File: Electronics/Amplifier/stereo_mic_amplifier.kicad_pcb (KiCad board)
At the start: 2 copper layers, 34.2 x 45.3 mm, 26 parts, among them P1 mic_L, P2 mic_R, P3 batt, P4 CONN_01X03, U1 TL072

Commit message: Updated layout & cnc files
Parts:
- moved C1 71.1 mm to (37.7, 35.7)
- moved C2 71.1 mm to (58.0, 58.5)
- moved C6 71.1 mm to (37.7, 50.9)
- moved C7 71.1 mm to (47.2, 57.1)
- moved C8 71.1 mm to (51.2, 69.8)
- moved D1 71.1 mm to (40.0, 57.0)
- moved D2 71.1 mm to (65.8, 57.4)
- moved P1 71.1 mm to (46.9, 34.7)
- moved P2 71.1 mm to (47.1, 63.1)
- moved P3 71.1 mm to (38.0, 60.8)
- moved P4 71.1 mm to (56.8, 71.5)
- moved R1 71.1 mm to (42.3, 46.2)
- moved R2 71.1 mm to (48.5, 60.1)
- moved R5 71.1 mm to (39.9, 69.1)
- moved R8 71.1 mm to (43.7, 69.2)
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
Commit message: rotated gerber
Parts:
- moved C1 39.6 mm to (41.0, 75.1), turned to 270 degrees
- moved R5 34.7 mm to (74.4, 73.0), turned to 0 degrees
- moved C3 33.6 mm to (48.6, 75.1), turned to 270 degrees
- moved P1 32.1 mm to (39.9, 66.0), turned to 0 degrees
- moved P3 31.4 mm to (66.1, 74.9), turned to 180 degrees
- moved R8 30.8 mm to (74.5, 69.2), turned to 180 degrees
- moved C6 30.4 mm to (56.2, 75.1), turned to 270 degrees
- moved D1 27.3 mm to (62.3, 72.8), turned to 90 degrees
- moved C4 26.8 mm to (40.4, 57.5), turned to 270 degrees
- moved R1 26.0 mm to (51.5, 70.5), turned to 180 degrees
- moved C8 25.3 mm to (75.1, 61.7), turned to 0 degrees
- moved P4 25.3 mm to (76.8, 56.1), turned to 180 degrees
- moved R4 25.0 mm to (48.2, 67.8), turned to 180 degrees
- moved R9 23.4 mm to (74.6, 48.1), turned to 0 degrees
- moved P2 21.4 mm to (68.4, 65.7), turned to 180 degrees
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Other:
- board size 34.2 x 45.3 mm -> 45.3 x 34.2 mm

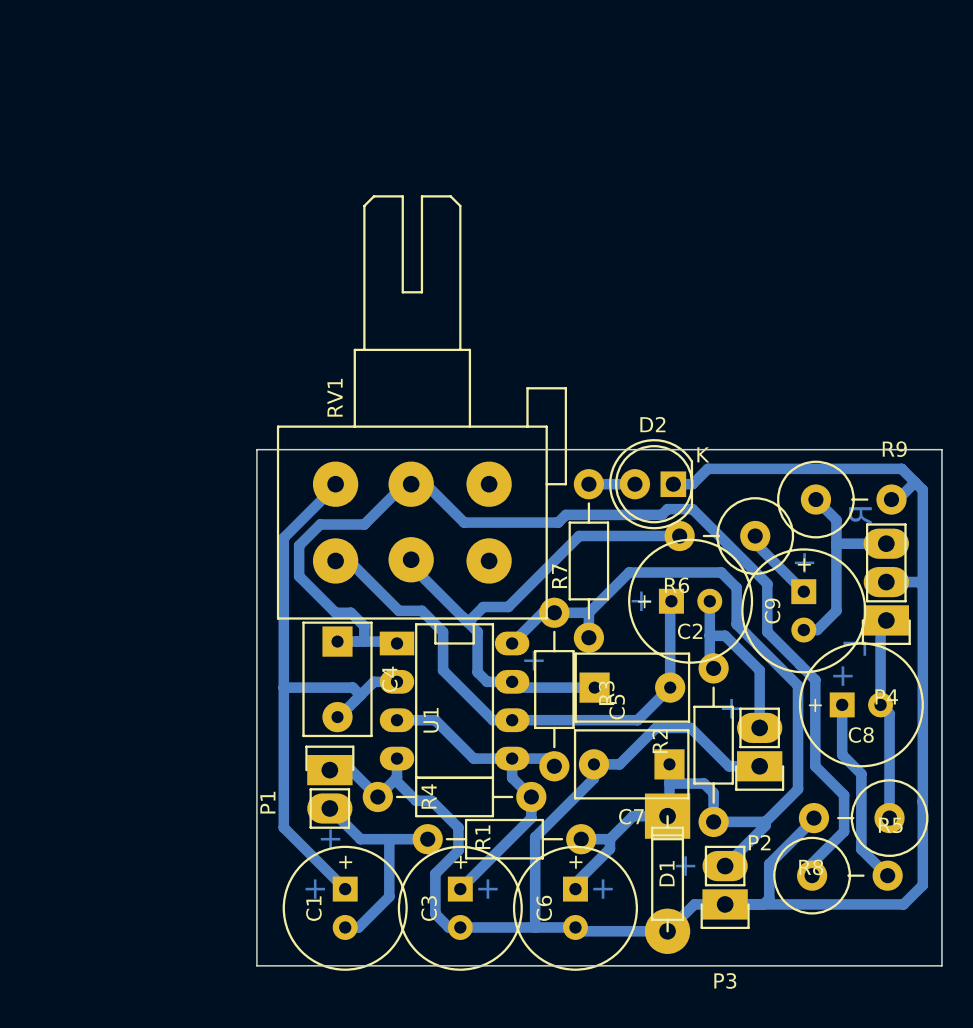
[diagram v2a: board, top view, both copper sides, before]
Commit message: Swapped misplaced capacitor values
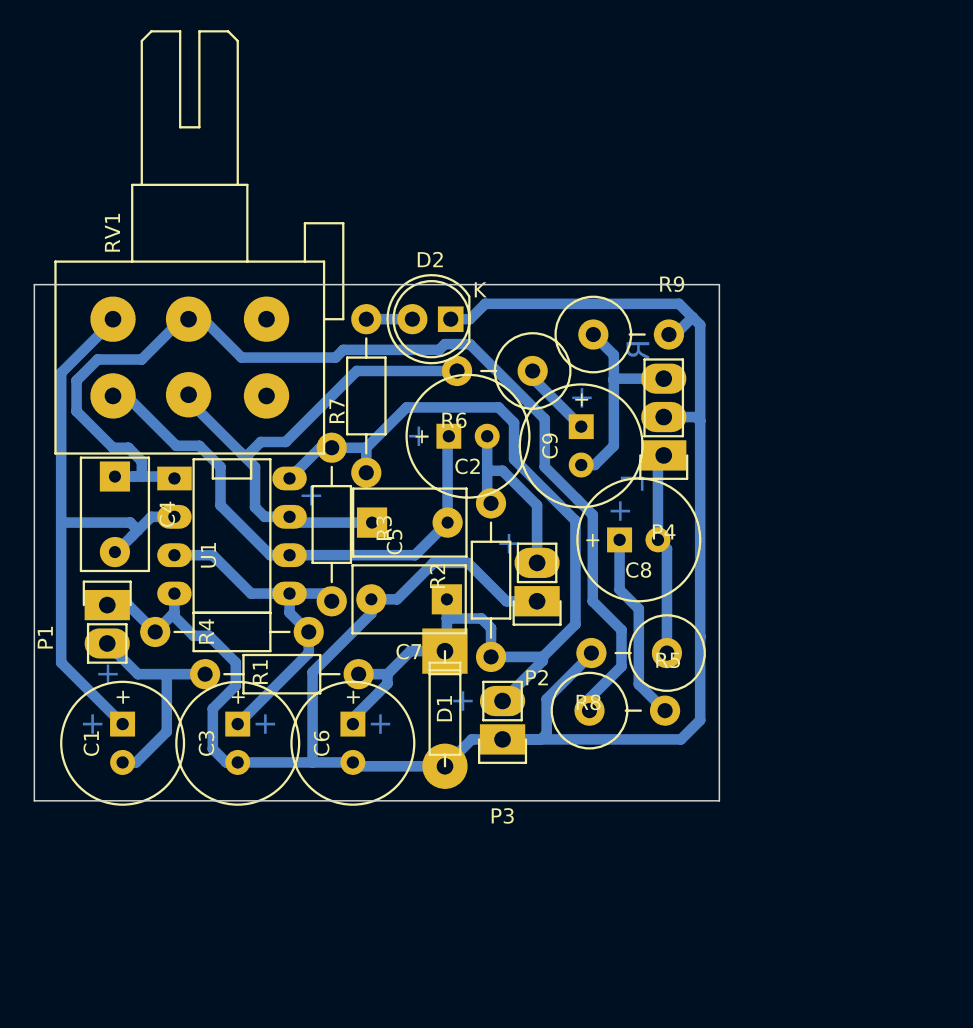
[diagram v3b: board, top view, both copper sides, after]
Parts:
- moved C1 18.3 mm to (26.2, 64.2)
- moved C3 18.3 mm to (33.8, 64.2)
- moved C6 18.3 mm to (41.5, 64.2)
- moved P4 18.3 mm to (62.0, 45.1)
- moved R5 18.3 mm to (59.6, 62.0)
- moved C8 18.3 mm to (60.4, 50.7)
- moved C9 18.3 mm to (56.6, 44.5)
- moved C4 18.3 mm to (25.7, 46.5)
- moved C5 18.3 mm to (42.7, 49.6)
- moved C7 18.3 mm to (47.7, 54.7)
- moved D1 18.3 mm to (47.6, 61.9)
- moved P1 18.3 mm to (25.2, 55.1)
- moved P3 18.3 mm to (51.4, 63.9)
- moved R1 18.3 mm to (36.8, 59.6)
- moved R2 18.3 mm to (50.6, 53.4)
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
